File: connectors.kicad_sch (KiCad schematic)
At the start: 15 parts, among them J1 Compute-Module-4_Plug_Connect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, Q3 DZDH0401DW, Q9 AO3401A, U20 NTS0102_XSON, U21 NTS0102_XSON

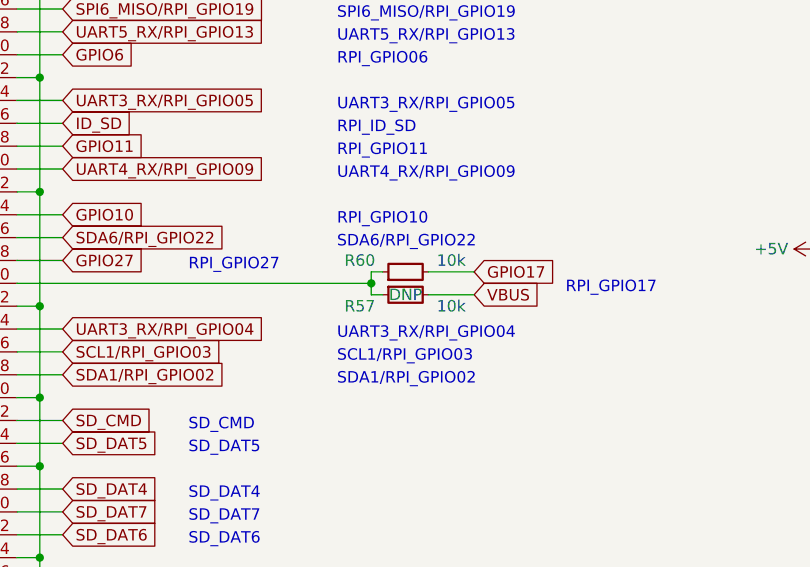
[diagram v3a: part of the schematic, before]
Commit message: [#56715] Change resistor size, USB VDDIO and reset
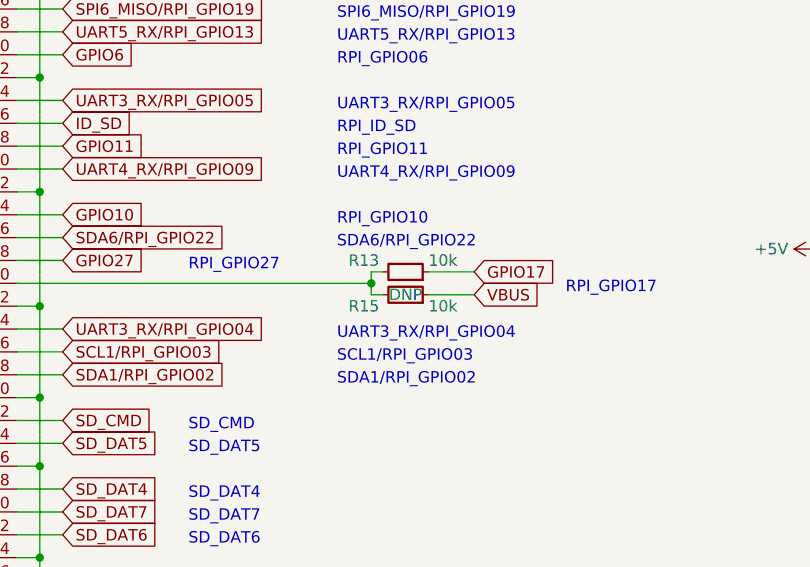
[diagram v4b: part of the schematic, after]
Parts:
- removed R57, R60: R_10k_0603, antmicro-footprints:R_0603_1608Metric, symbol antmicroResistors0603:R_10k_0603
- added R13, R15: R_10k_0402, antmicro-footprints:R_0402_1005Metric, symbol antmicroResistors0402:R_10k_0402
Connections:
- net GPIO17: now also R13.1
- net VBUS: now also R15.1
- net at J1.50: now also R13.2, R15.2
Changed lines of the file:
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@@
-    )
-  )
-  (symbol (lib_id "antmicroResistors0603:R_10k_0603") (at 165.1 140.97 0) (unit 1)
-    (in_bom yes) (on_board yes) (dnp no)
-    (property "Reference" "R57" (at 162.56 142.24 0)
-      (effects (font (size 1.27 1.27) (thickness 0.15)))
-    )
-    (property "Value" "R_10k_0603" (at 185.42 153.67 0)
-      (effects (font (size 1.27 1.27) (thickness 0.15)) (justify left bottom) hide)
-    )
-    (property "Footprint" "antmicro-footprints:R_0603_1608Metric" (at 185.42 156.21 0)
-      (effects (font (size 1.27 1.27) (thickness 0.15)) (justify left bottom) hide)
-    )
-    (property "Datasheet" "https://www.bourns.com/docs/product-datasheets/cr.pdf" (at 185.42 158.75 0)
-      (effects (font (size 1.27 1.27) (thickness 0.15)) (justify left bottom) hide)
-    )
-    (property "MPN" "CR0603-FX-1002ELF" (at 185.42 161.29 0)
-      (effects (font (size 1.27 1.27) (thickness 0.15)) (justify left bottom) hide)
-    )
-    (property "Manufacturer" "Bourns" (at 185.42 163.83 0)
-      (effects (font (size 1.27 1.27) (thickness 0.15)) (justify left bottom) hide)
-    )
-    (property "License" "Apache-2.0" (at 185.42 166.37 0)
-      (effects (font (size 1.27 1.27) (thickness 0.15)) (justify left bottom) hide)
-    )
-    (property "Author" "Antmicro" (at 185.42 168.91 0)
-      (effects (font (size 1.27 1.27) (thickness 0.15)) (justify left bottom) hide)
-    )
-    (property "Val" "10k" (at 172.72 142.24 0)
-      (effects (font (size 1.27 1.27) (thickness 0.15)))
-    )
-    (property "Tolerance" "1%" (at 185.42 151.13 0)
-      (effects (font (size 1.27 1.27)) (justify left bottom) hide)
-    )
-    (property "DNP" "DNP" (at 167.64 140.97 0)
-      (effects (font (size 1.27 1.27)))
-    )
-    (pin "2")
-    (pin "1")
-    (instances
-      (project "polarfire-som"
-        (path "/db4a0d3e-2eb3-499e-977d-6eb378cfd3ed/1a89b4c6-5d95-4c13-8da9-62b42c0a8ed9"
-          (reference "R57") (unit 1)
-        )
-      )
     )
   )
@@
         (path "/db4a0d3e-2eb3-499e-977d-6eb378cfd3ed/1a89b4c6-5d95-4c13-8da9-62b42c0a8ed9"
           (reference "#PWR0213") (unit 1)
-        )
-      )
-    )
-  )
-  (symbol (lib_id "antmicroResistors0603:R_10k_0603") (at 165.1 138.43 0) (mirror x) (unit 1)
-    (in_bom yes) (on_board yes) (dnp no)
-    (property "Reference" "R60" (at 162.56 137.16 0)
-      (effects (font (size 1.27 1.27) (thickness 0.15)))
-    )
-    (property "Value" "R_10k_0603" (at 185.42 125.73 0)
-      (effects (font (size 1.27 1.27) (thickness 0.15)) (justify left bottom) hide)
-    )
-    (property "Footprint" "antmicro-footprints:R_0603_1608Metric" (at 185.42 123.19 0)
-      (effects (font (size 1.27 1.27) (thickness 0.15)) (justify left bottom) hide)
-    )
-    (property "Datasheet" "https://www.bourns.com/docs/product-datasheets/cr.pdf" (at 185.42 120.65 0)
-      (effects (font (size 1.27 1.27) (thickness 0.15)) (justify left bottom) hide)
-    )
-    (property "MPN" "CR0603-FX-1002ELF" (at 185.42 118.11 0)
-      (effects (font (size 1.27 1.27) (thickness 0.15)) (justify left bottom) hide)
-    )
-    (property "Manufacturer" "Bourns" (at 185.42 115.57 0)
-      (effects (font (size 1.27 1.27) (thickness 0.15)) (justify left bottom) hide)
-    )
-    (property "License" "Apache-2.0" (at 185.42 113.03 0)
-      (effects (font (size 1.27 1.27) (thickness 0.15)) (justify left bottom) hide)
-    )
-    (property "Author" "Antmicro" (at 185.42 110.49 0)
-      (effects (font (size 1.27 1.27) (thickness 0.15)) (justify left bottom) hide)
-    )
-    (property "Val" "10k" (at 172.72 137.16 0)
-      (effects (font (size 1.27 1.27) (thickness 0.15)))
-    )
-    (property "Tolerance" "1%" (at 185.42 128.27 0)
-      (effects (font (size 1.27 1.27)) (justify left bottom) hide)
-    )
-    (pin "2")
-    (pin "1")
-    (instances
-      (project "polarfire-som"
-        (path "/db4a0d3e-2eb3-499e-977d-6eb378cfd3ed/1a89b4c6-5d95-4c13-8da9-62b42c0a8ed9"
-          (reference "R60") (unit 1)
         )
       )
@@
     )
   )
+  (symbol (lib_id "antmicroResistors0402:R_10k_0402") (at 170.18 138.43 180) (unit 1)
+    (in_bom yes) (on_board yes) (dnp no)
+    (property "Reference" "R13" (at 161.29 137.16 0)
+      (effects (font (size 1.27 1.27) (thickness 0.15)) (justify right))
+    )
+    (property "Value" "R_10k_0402" (at 149.86 125.73 0)
+      (effects (font (size 1.27 1.27) (thickness 0.15)) (justify left bottom) hide)
+    )
+    (property "Footprint" "antmicro-footprints:R_0402_1005Metric" (at 149.86 123.19 0)
+      (effects (font (size 1.27 1.27) (thickness 0.15)) (justify left bottom) hide)
+    )
+    (property "Datasheet" "https://www.bourns.com/docs/product-datasheets/cr.pdf" (at 149.86 120.65 0)
+      (effects (font (size 1.27 1.27) (thickness 0.15)) (justify left bottom) hide)
+    )
+    (property "MPN" "CR0402-FX-1002GLF" (at 149.86 118.11 0)
+      (effects (font (size 1.27 1.27) (thickness 0.15)) (justify left bottom) hide)
+    )
+    (property "Manufacturer" "Bourns" (at 149.86 115.57 0)
+      (effects (font (size 1.27 1.27) (thickness 0.15)) (justify left bottom) hide)
+    )
+    (property "License" "Apache-2.0" (at 149.86 113.03 0)
+      (effects (font (size 1.27 1.27) (thickness 0.15)) (justify left bottom) hide)
+    )
+    (property "Author" "Antmicro" (at 149.86 110.49 0)
+      (effects (font (size 1.27 1.27) (thickness 0.15)) (justify left bottom) hide)
+    )
+    (property "Val" "10k" (at 170.18 137.16 0)
+      (effects (font (size 1.27 1.27) (thickness 0.15)) (justify right))
+    )
+    (property "Tolerance" "1%" (at 149.86 128.27 0)
+      (effects (font (size 1.27 1.27)) (justify left bottom) hide)
+    )
+    (pin "1")
+    (pin "2")
+    (instances
+      (project "polarfire-som"
+        (path "/db4a0d3e-2eb3-499e-977d-6eb378cfd3ed/1a89b4c6-5d95-4c13-8da9-62b42c0a8ed9"
+          (reference "R13") (unit 1)
+        )
+      )
+    )
+  )
   (symbol (lib_id "antmicroCapacitors0402:C_100n_0402") (at 175.26 247.65 270) (unit 1)
     (in_bom yes) (on_board yes) (dnp no)
@@
         )
       )
+    )
+  )
+  (symbol (lib_id "antmicroResistors0402:R_10k_0402") (at 170.18 140.97 180) (unit 1)
+    (in_bom yes) (on_board yes) (dnp no)
+    (property "Reference" "R15" (at 161.29 142.24 0)
+      (effects (font (size 1.27 1.27) (thickness 0.15)) (justify right))
+    )
+    (property "Value" "R_10k_0402" (at 149.86 128.27 0)
+      (effects (font (size 1.27 1.27) (thickness 0.15)) (justify left bottom) hide)
+    )
+    (property "Footprint" "antmicro-footprints:R_0402_1005Metric" (at 149.86 125.73 0)
+      (effects (font (size 1.27 1.27) (thickness 0.15)) (justify left bottom) hide)
+    )
+    (property "Datasheet" "https://www.bourns.com/docs/product-datasheets/cr.pdf" (at 149.86 123.19 0)
+      (effects (font (size 1.27 1.27) (thickness 0.15)) (justify left bottom) hide)
+    )
+    (property "MPN" "CR0402-FX-1002GLF" (at 149.86 120.65 0)
+      (effects (font (size 1.27 1.27) (thickness 0.15)) (justify left bottom) hide)
+    )
+    (property "Manufacturer" "Bourns" (at 149.86 118.11 0)
+      (effects (font (size 1.27 1.27) (thickness 0.15)) (justify left bottom) hide)
+    )
+    (property "License" "Apache-2.0" (at 149.86 115.57 0)
+      (effects (font (size 1.27 1.27) (thickness 0.15)) (justify left bottom) hide)
+    )
+    (property "Author" "Antmicro" (at 149.86 113.03 0)
+      (effects (font (size 1.27 1.27) (thickness 0.15)) (justify left bottom) hide)
+    )
+    (property "Val" "10k" (at 170.18 142.24 0)
+      (effects (font (size 1.27 1.27) (thickness 0.15)) (justify right))
+    )
+    (property "Tolerance" "1%" (at 149.86 130.81 0)
+      (effects (font (size 1.27 1.27)) (justify left bottom) hide)
+    )
+    (property "DNP" "DNP" (at 167.64 140.97 0)
+      (effects (font (size 1.27 1.27)))
+    )
+    (pin "1")
+    (pin "2")
+    (instances
+      (project "polarfire-som"
+        (path "/db4a0d3e-2eb3-499e-977d-6eb378cfd3ed/1a89b4c6-5d95-4c13-8da9-62b42c0a8ed9"
+          (reference "R15") (unit 1)
+        )
+      )

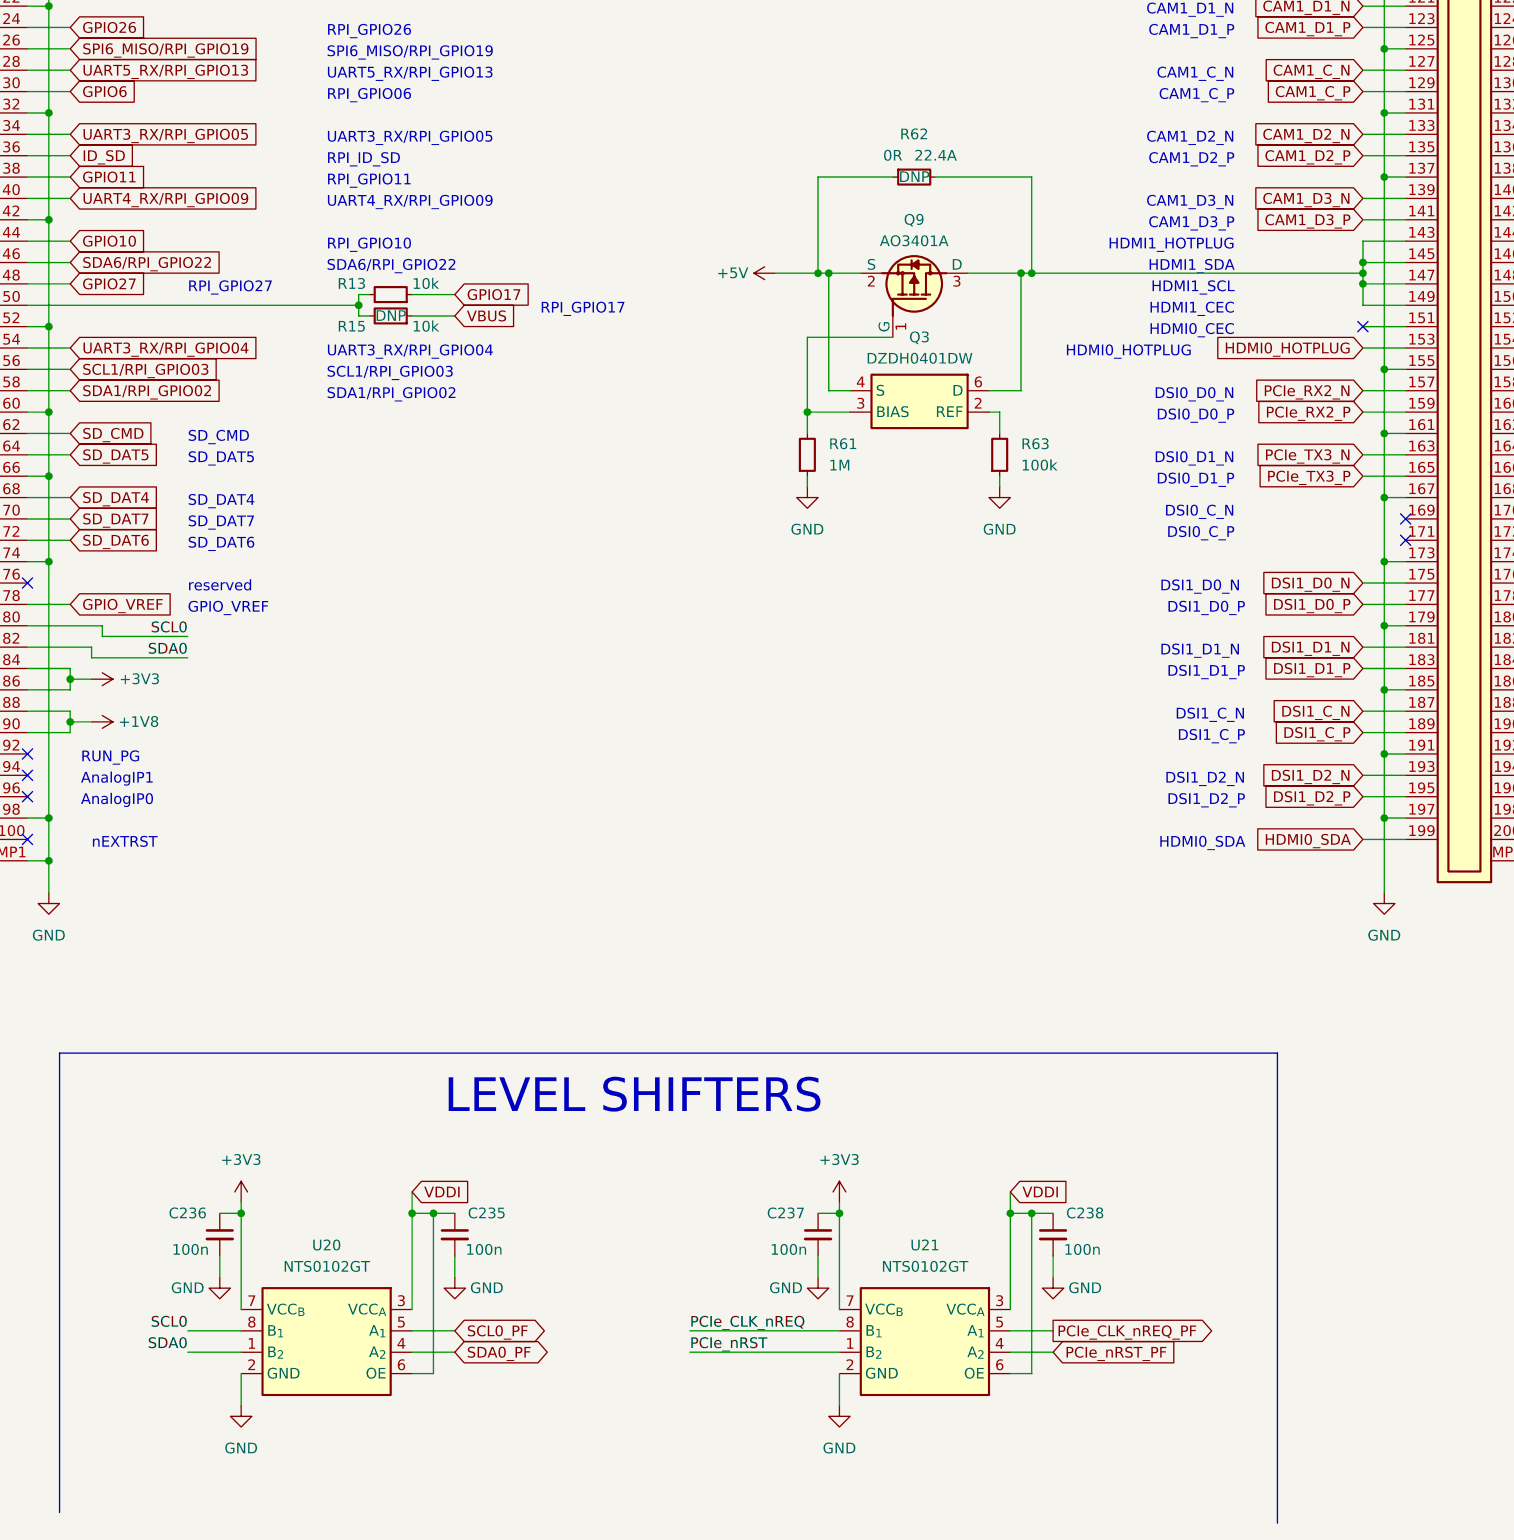
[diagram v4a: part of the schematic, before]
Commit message: [#56952] Place top designators, clean ERC
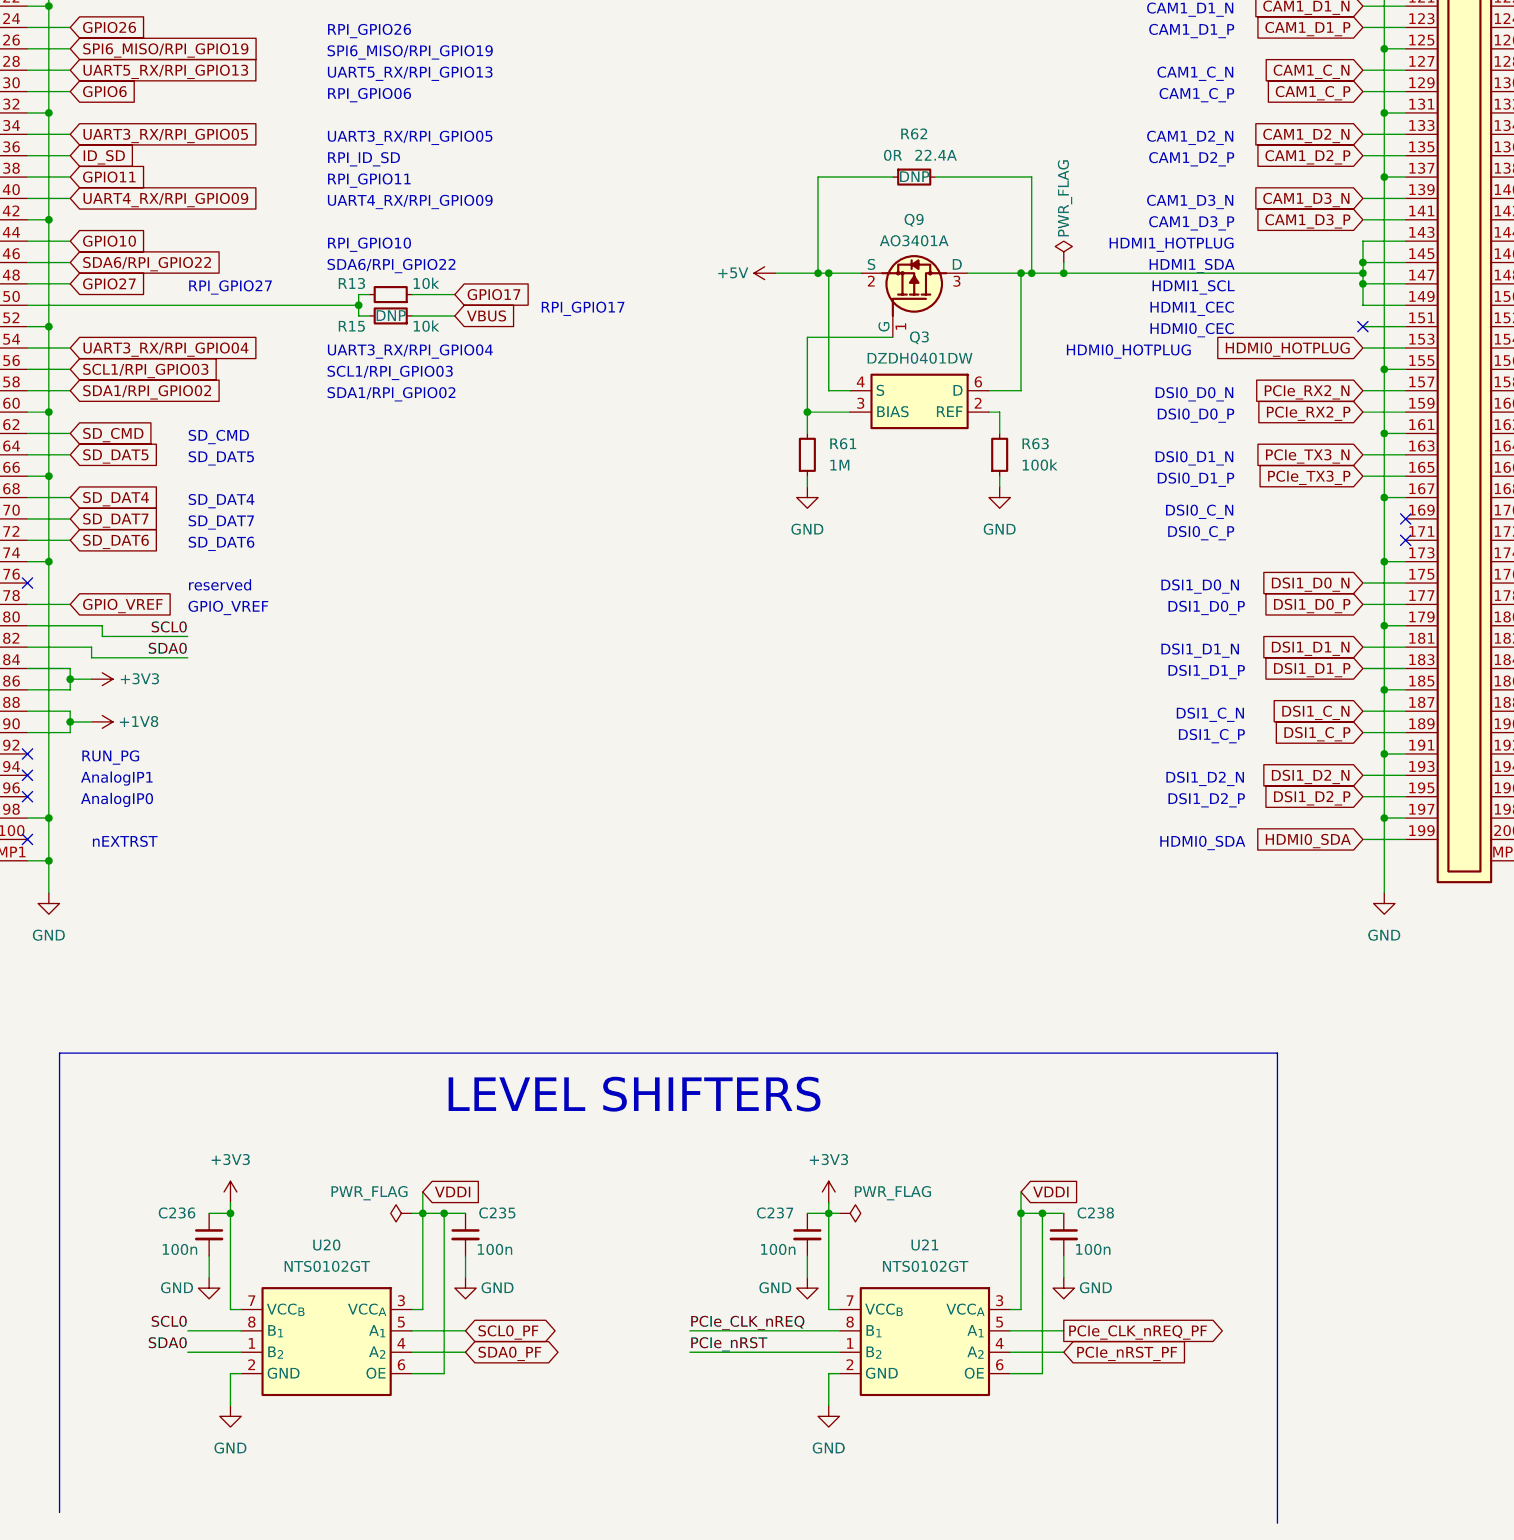
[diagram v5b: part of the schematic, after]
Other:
- moved on the sheet: C235, C236, C237, C238
